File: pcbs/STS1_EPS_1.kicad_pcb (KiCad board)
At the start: 4 copper layers, 114.3 x 55.9 mm, 7 parts, among them J1 Conn_02x06_Counter_Clockwise, J2 Conn_02x06_Counter_Clockwise, Q1 SI7272DP-T1-GE3, Q2 SI7135DP-T1-GE3, U1 LTC4020EUHFPBF, U2 BQ29209DRBT, U3 MAX11632EEGT

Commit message: Worked on STS1_EPS.
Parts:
- removed J2: Conn_02x06_Counter_Clockwise, STS_Connector:M808661205
- removed Q1: SI7272DP-T1-GE3, STS_Package_SO:POWERPAK_SO8
- removed Q2: SI7135DP-T1-GE3, STS_Package_SO:POWERPAK_SO8_single
- removed U2: BQ29209DRBT, STS_Package_VSON:TI_VSON8
- removed U3: MAX11632EEGT, STS_Package_QSOP:MAX_QSOP24
- added C1: 220µ, Capacitor_Tantalum_SMD:CP_EIA-3528-12_Kemet-T, F.Cu at (239.2, 69.1)
- added C10: 680p, Capacitor_SMD:C_0805_2012Metric, F.Cu at (243.0, 72.7)
- added C11: 330n, Capacitor_SMD:C_0805_2012Metric, F.Cu at (247.4, 71.7)
- added C2: 1µ, Capacitor_SMD:C_0805_2012Metric, F.Cu at (237.0, 80.7)
- added C3: 1µ, Capacitor_SMD:C_0805_2012Metric, F.Cu at (250.0, 68.4)
- added C5: 220µ, Capacitor_Tantalum_SMD:CP_EIA-3528-12_Kemet-T, F.Cu at (232.1, 74.0)
- added C6: 2µ2, Capacitor_SMD:C_0805_2012Metric, F.Cu at (241.4, 76.7)
- added C7: 10µ, Capacitor_SMD:C_0805_2012Metric, F.Cu at (231.3, 84.1)
- added C8: 200n, Capacitor_SMD:C_1812_4532Metric, F.Cu at (232.6, 69.4)
- added C9: 680p, Capacitor_SMD:C_0805_2012Metric, F.Cu at (231.3, 81.1)
- added CSBI_1: Conn_02x25_Odd_Even, Connector_PinHeader_2.00mm:PinHeader_2x25_P2.00mm_Vertical, F.Cu at (118.5, 64.3)
- added CSBI_2: Conn_02x25_Odd_Even, Connector_PinHeader_2.00mm:PinHeader_2x25_P2.00mm_Vertical, F.Cu at (192.6, 64.3)
- added D1: SD1206T040S1R0, Diode_SMD:D_1206_3216Metric, F.Cu at (237.9, 73.5)
- added D2: SD1206T040S1R0, Diode_SMD:D_1206_3216Metric, F.Cu at (232.0, 77.9)
- added D3: LED, LED_SMD:LED_0805_2012Metric, F.Cu at (235.8, 83.8)
- added D4: LED, LED_SMD:LED_0805_2012Metric, F.Cu at (237.0, 77.7)
- added H1: MountingHole_Pad, MountingHole:MountingHole_4.3mm_M4_Pad_Via, F.Cu at (120.6, 46.3)
- added H2: MountingHole_Pad, MountingHole:MountingHole_4.3mm_M4_Pad_Via, F.Cu at (192.6, 46.3)
- added H3: MountingHole_Pad, MountingHole:MountingHole_4.3mm_M4_Pad_Via, F.Cu at (120.6, 122.3)
- added H4: MountingHole_Pad, MountingHole:MountingHole_4.3mm_M4_Pad_Via, F.Cu at (192.6, 122.3)
- added J3: Panel X-, STS_Connector:M808661205, F.Cu at (164.4, 62.3)
- added R1: 17k8, Resistor_SMD:R_0805_2012Metric, F.Cu at (251.9, 74.3)
- added R10: 1k, Resistor_SMD:R_0805_2012Metric, F.Cu at (254.4, 68.4)
- added R11: 1k, Resistor_SMD:R_0805_2012Metric, F.Cu at (250.2, 77.6)
- added R13: 200k, Resistor_SMD:R_0805_2012Metric, F.Cu at (245.8, 79.7)
- added R18: 100, Resistor_SMD:R_0805_2012Metric, F.Cu at (250.2, 80.6)
- added R19: 100, Resistor_SMD:R_0805_2012Metric, F.Cu at (256.3, 71.3)
- added R2: 100k, Resistor_SMD:R_0805_2012Metric, F.Cu at (241.4, 79.7)
- added R20: 10m, Resistor_SMD:R_1206_3216Metric, F.Cu at (245.0, 68.5)
- added R3: 28k, Resistor_SMD:R_0805_2012Metric, F.Cu at (247.4, 74.7)
- added R4: 100k, Resistor_SMD:R_0805_2012Metric, F.Cu at (244.6, 82.7)
- added R5: 31k, Resistor_SMD:R_0805_2012Metric, F.Cu at (256.3, 74.3)
- added R6: 100k, Resistor_SMD:R_0805_2012Metric, F.Cu at (251.9, 71.4)
- added R7: 500k, Resistor_SMD:R_0805_2012Metric, F.Cu at (240.2, 83.7)
- added R9: 200k, Resistor_SMD:R_0805_2012Metric, F.Cu at (258.8, 68.4)
- added U4: BQ29209DRBT, STS_Package_VSON:TI_VSON8, B.Cu at (158.1, 101.3)
- J1: value Conn_02x06_Counter_Clockwise -> Panel X+
- U1: value LTC4020EUHFPBF -> coordinate_system; footprint STS_Package_DFN_QFN:AD_QFN-38_UHF -> STS:Coordinates
- moved J1 68.5 mm to (175.1, 81.8), turned to 0 degrees
- moved U1 49.2 mm to (167.6, 54.9)
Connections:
- J1 pad 1: unconnected-(J1-Pad1) -> /Panel_X+_1
- J1 pad 10: unconnected-(J1-Pad10) -> /Panel_X+_10
- J1 pad 11: unconnected-(J1-Pad11) -> /Panel_X+_11
- J1 pad 12: unconnected-(J1-Pad12) -> /Panel_X+_12
- J1 pad 2: unconnected-(J1-Pad2) -> /Panel_X+_2
- J1 pad 3: unconnected-(J1-Pad3) -> /Solar Cell Connectors/Panel_X-.MPPT3
- J1 pad 4: unconnected-(J1-Pad4) -> /Panel_X+_4
- J1 pad 5: unconnected-(J1-Pad5) -> /Panel_X+_5
- J1 pad 6: unconnected-(J1-Pad6) -> /Panel_X+_6
- J1 pad 7: unconnected-(J1-Pad7) -> /Panel_X+_7
- J1 pad 8: unconnected-(J1-Pad8) -> /Panel_X+_8
- J1 pad 9: unconnected-(J1-Pad9) -> /Panel_X+_9
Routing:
- net Net-(CSBI_2-Pad13): track 0.00 -> 2.00 mm
- net Net-(CSBI_2-Pad11): track 0.00 -> 2.00 mm
- net Net-(CSBI_1-Pad31): track 0.00 -> 2.00 mm
- net Net-(CSBI_1-Pad29): track 0.00 -> 2.00 mm
- net Net-(CSBI_1-Pad27): track 0.00 -> 2.00 mm
- net Net-(CSBI_1-Pad25): track 0.00 -> 2.00 mm
- net /STS1_connector/UCI_COBC_UART_2: track 0.00 -> 2.00 mm
- net /STS1_connector/UCI_COBC_UART_1: track 0.00 -> 2.00 mm
- net /STS1_connector/UCI_COBC_3V3: track 0.00 -> 2.00 mm
- net /STS1_connector/UART_COBC_EDU_2: track 0.00 -> 2.00 mm
- net /STS1_connector/UART_COBC_EDU_1: track 0.00 -> 2.00 mm
- net /STS1_connector/EPS_CHARGING: track 0.00 -> 2.00 mm
- net /STS1_connector/EPS_BAT_GOOD: track 0.00 -> 2.00 mm
- net /STS1_connector/EPS_ANT_DEPLOYED: track 0.00 -> 2.00 mm
- net /STS1_connector/EDU_UPDATE: track 0.00 -> 2.00 mm
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- added copper zone on In1.Cu, net GND
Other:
- board size 114.3 x 55.9 mm -> 81 x 85 mm
- rule pad_to_mask_clearance: 0 -> 0.19
- board text added: "ID:"
- board text added: "TU Wien Space Team STS [PCB name] [Version]"

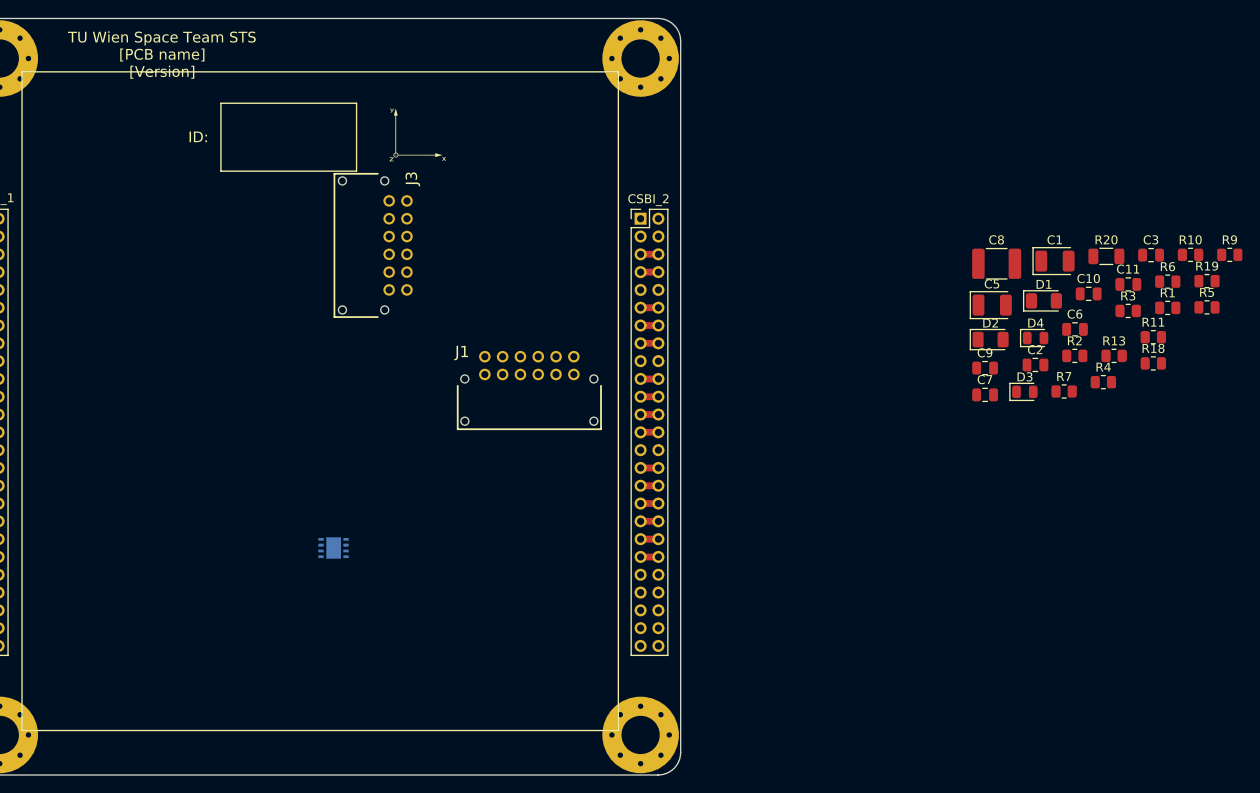
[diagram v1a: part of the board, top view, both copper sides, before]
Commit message: Worked on STS1_EPS_1.
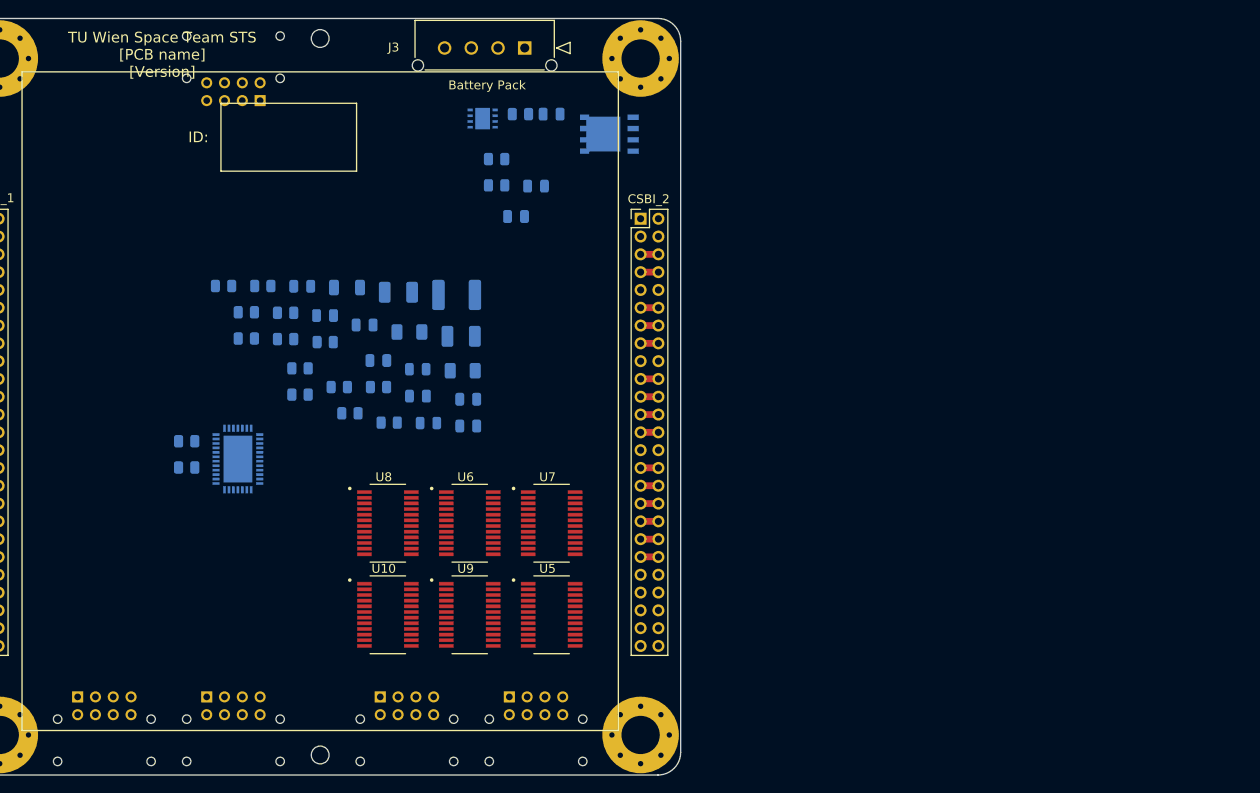
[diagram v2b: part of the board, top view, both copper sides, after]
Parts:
- removed J1: Panel X+, STS_Connector:M808661205
- added C12: 100n, Capacitor_SMD:C_0805_2012Metric, B.Cu at (178.6, 64.0)
- added C13: 100n, Capacitor_SMD:C_0805_2012Metric, B.Cu at (182.6, 52.5)
- added C13: 100n, Capacitor_SMD:C_0805_2012Metric, B.Cu at (180.9, 60.6)
- added J2: Panel X+, STS_Connector:M8085108, B.Cu at (163.4, 118.0)
- added J4: Panel X-, STS_Connector:M8085108, B.Cu at (143.9, 118.0)
- added J5: Panel Y+, STS_Connector:M8085108, B.Cu at (129.4, 118.0)
- added J6: Panel Y-, STS_Connector:M8085108, B.Cu at (149.9, 51.0)
- added J7: Panel Z+, STS_Connector:M8085108, B.Cu at (177.9, 118.0)
- added Q1: SI7135DP-T1-GE3, STS_Package_SO:POWERPAK_SO8_single, B.Cu at (189.1, 54.8)
- added R16: R, Resistor_SMD:R_0805_2012Metric, B.Cu at (141.6, 89.3)
- added R17: R, Resistor_SMD:R_0805_2012Metric, B.Cu at (141.6, 92.2)
- added R21: 100, Resistor_SMD:R_0805_2012Metric, B.Cu at (176.5, 57.6)
- added R22: 140, Resistor_SMD:R_0805_2012Metric, B.Cu at (176.5, 60.5)
- added R23: 140, Resistor_SMD:R_0805_2012Metric, B.Cu at (179.1, 52.5)
- added U10: MAX11632EEGT, STS_Package_QSOP:MAX_QSOP24, F.Cu at (164.2, 108.8)
- added U5: MAX11632EEGT, STS_Package_QSOP:MAX_QSOP24, F.Cu at (182.6, 108.8)
- added U6: MAX11632EEGT, STS_Package_QSOP:MAX_QSOP24, F.Cu at (173.4, 98.5)
- added U7: MAX11632EEGT, STS_Package_QSOP:MAX_QSOP24, F.Cu at (182.6, 98.5)
- added U8: MAX11632EEGT, STS_Package_QSOP:MAX_QSOP24, F.Cu at (164.2, 98.5)
- added U9: MAX11632EEGT, STS_Package_QSOP:MAX_QSOP24, F.Cu at (173.4, 108.8)
- C1, C10, C11, C2, C3, C5, C6, C7, C8, C9, D1, D2, D3, D4, R1, R10, R11, R13, R18, R19, R2, R20, R3, R4, R5, R6, R7, R9: moved to B.Cu
- J3: value Panel X- -> Battery Pack; footprint STS_Connector:M808661205 -> STS_Connector:436500415
- U1: value coordinate_system -> LTC4020EUHFPBF; footprint STS:Coordinates -> STS_Package_DFN_QFN:AD_QFN-38_UHF; moved to B.Cu
- moved R9 113.1 mm to (145.8, 71.9), turned to 180 degrees
- moved R19 108.0 mm to (148.3, 74.8), turned to 180 degrees
- moved R5 108.0 mm to (148.3, 77.8), turned to 180 degrees
- moved R10 104.3 mm to (150.2, 71.9), turned to 180 degrees
- moved R1 99.2 mm to (152.7, 77.8), turned to 180 degrees
- moved R6 99.2 mm to (152.7, 74.9), turned to 180 degrees
- moved R11 95.9 mm to (154.4, 81.1), turned to 180 degrees
- moved R18 95.9 mm to (154.4, 84.1), turned to 180 degrees
- moved C3 95.4 mm to (154.6, 71.9), turned to 180 degrees
- moved C11 90.3 mm to (157.2, 75.2), turned to 180 degrees
- moved R3 90.3 mm to (157.2, 78.2), turned to 180 degrees
- moved R13 87.1 mm to (158.8, 83.2), turned to 180 degrees
- moved R20 85.4 mm to (159.6, 72.0), turned to 180 degrees
- moved R4 84.7 mm to (160.0, 86.2), turned to 180 degrees
- moved C10 81.4 mm to (161.6, 76.2), turned to 180 degrees
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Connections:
- D3 pad 2: /Battery Charge Controller/Vout -> /Battery Charge Controller/VOUT
- D4 pad 2: /Battery Charge Controller/Vout -> /Battery Charge Controller/VOUT
- J3 pad 1: /Solar Cell Connectors/SC3_V+ -> /Battery Charge Controller/BATT
- J3 pad 2: /Solar Cell Connectors/SC1_I+ -> GND
- J3 pad 3: /Solar Cell Connectors/MPPT3 -> /Battery/NTC
- J3 pad 4: /Panel_X+_4 -> /Battery/CENTER
- U4 pad 1: unconnected-(U4-Pad1) -> /Battery/VC2
- U4 pad 2: unconnected-(U4-Pad2) -> /Battery/VC1
- U4 pad 3: unconnected-(U4-Pad3) -> /Battery/VC1_CB
- U4 pad 6: GND -> /Battery/BAT_FAULT
- U4 pad 7: /Battery/VOUT -> /Battery Charge Controller/BATT
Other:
- outline, holes or cut-outs redrawn

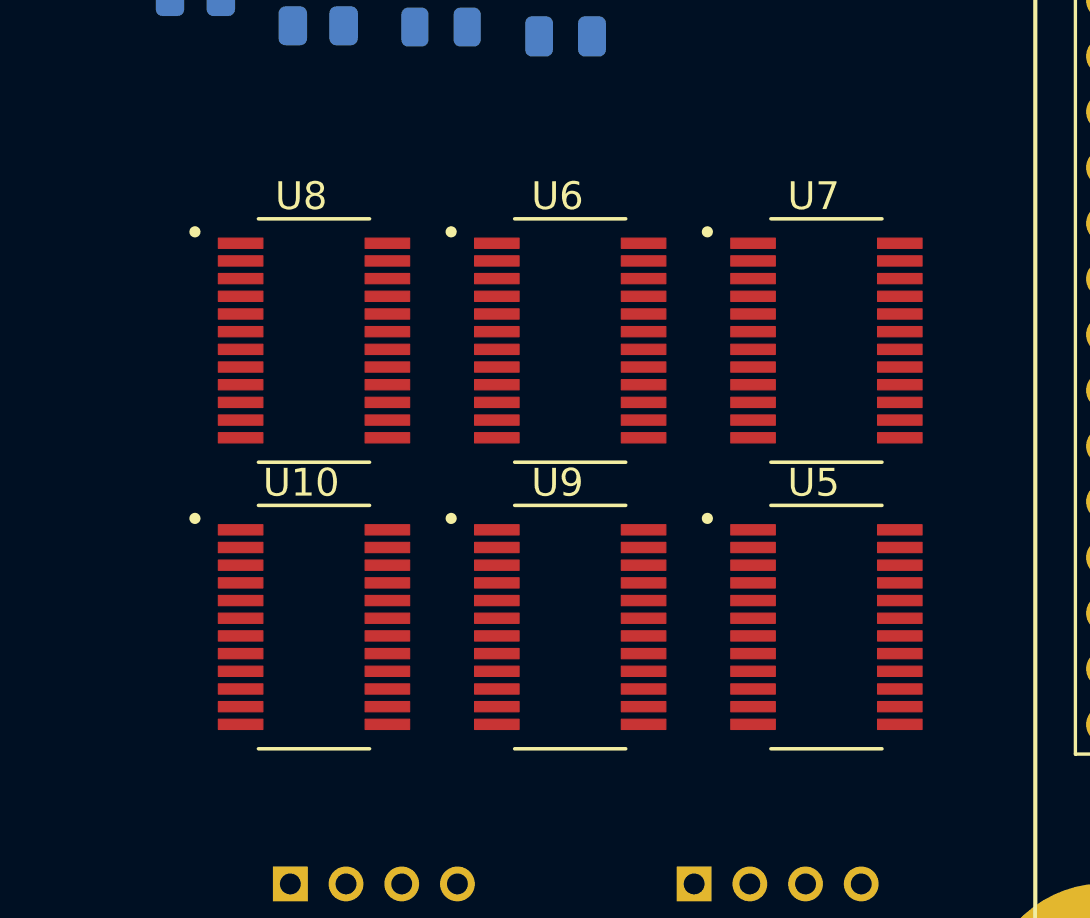
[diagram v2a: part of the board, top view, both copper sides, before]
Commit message: Worked on STS_EPS_1.
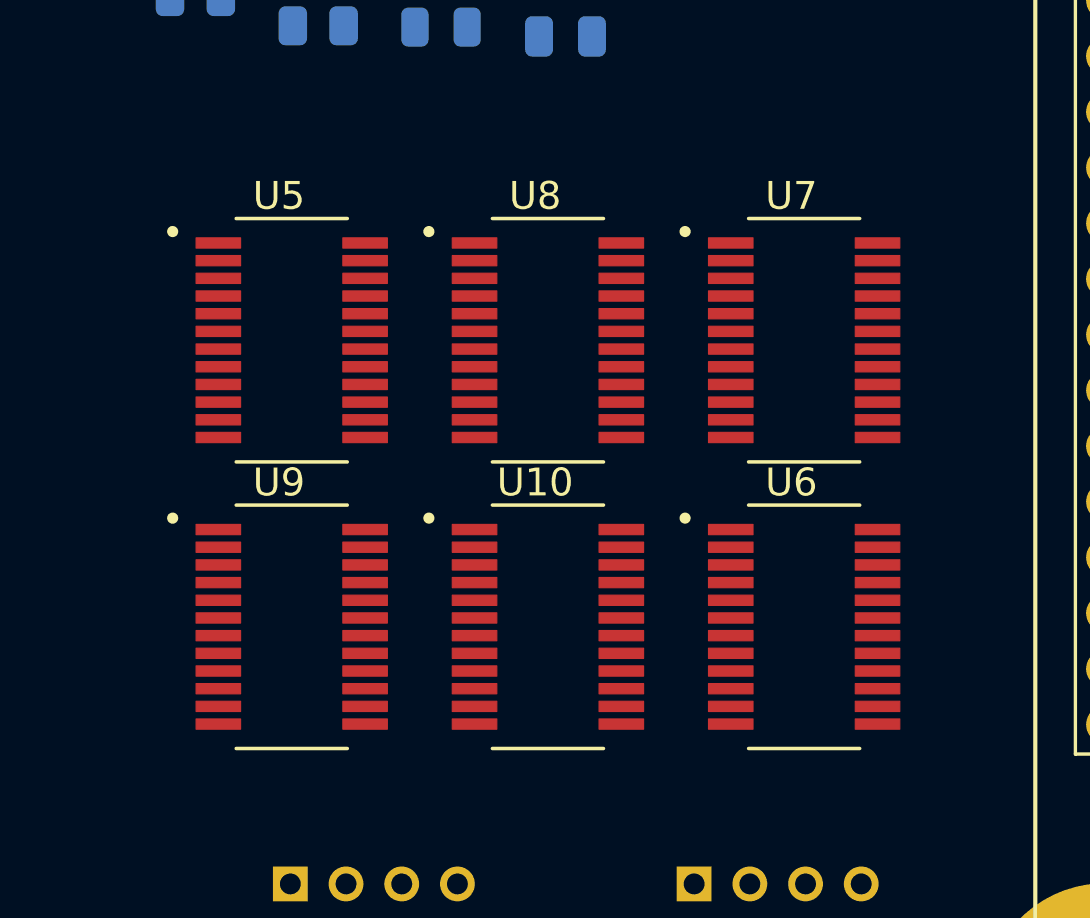
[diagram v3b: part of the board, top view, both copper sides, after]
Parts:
- moved U5 21.8 mm to (163.4, 98.5)
- moved U6 13.3 mm to (181.8, 108.8)
- moved U9 10.0 mm to (163.4, 108.8)
- moved U10 8.40 mm to (172.6, 108.8)
- moved U8 8.40 mm to (172.6, 98.5)
- moved U7 0.80 mm to (181.8, 98.5)
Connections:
- net /Battery Charge Controller/VOUT renamed /Analog Digital Converters/VOUT
- J2 pad 3: /Solar Cell Connectors/Panel_Y-_3 -> /Solar Cell Connectors/Panel_X+_3
- J2 pad 6: /Solar Cell Connectors/Panel_Y-_3 -> /Solar Cell Connectors/Panel_X+_6
- J4 pad 3: /Solar Cell Connectors/Panel_Y-_3 -> /Solar Cell Connectors/Panel_X-_3
- J4 pad 6: /Solar Cell Connectors/Panel_Y-_3 -> /Solar Cell Connectors/Panel_X-_6
- J5 pad 3: /Solar Cell Connectors/Panel_Y-_3 -> /Solar Cell Connectors/Panel_Y+_3
- J5 pad 6: /Solar Cell Connectors/Panel_Y-_3 -> /Solar Cell Connectors/Panel_Y+_6
- J6 pad 6: /Solar Cell Connectors/Panel_Y-_3 -> /Solar Cell Connectors/Panel_Y-_6
- J7 pad 3: /Solar Cell Connectors/Panel_Y-_3 -> /Solar Cell Connectors/Panel_Z+_3
- J7 pad 6: /Solar Cell Connectors/Panel_Y-_3 -> /Solar Cell Connectors/Panel_Z+_6
- U1 pad 36: /Solar Cell Connectors/Panel_Y-_3 -> /Panel_X+_3
- U10 pad 18: unconnected-(U10-Pad18) -> GND
- U5 pad 18: unconnected-(U5-Pad18) -> GND
- U5 pad 22: unconnected-(U5-Pad22) -> /Analog Digital Converters/Panel_X+_2
- U6 pad 18: unconnected-(U6-Pad18) -> GND
- U7 pad 18: unconnected-(U7-Pad18) -> GND
- U8 pad 18: unconnected-(U8-Pad18) -> GND
- U9 pad 18: unconnected-(U9-Pad18) -> GND
